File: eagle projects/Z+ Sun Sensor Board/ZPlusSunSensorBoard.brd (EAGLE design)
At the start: 78 x 78 mm, 54 parts, among them J1 Power In, J2 Power Out, U1 TSV991AILT, U2 ADS7841E_2K5, U4 LM20BIM7X_NOPB, U5 TSV991AILT, U8 TSV991AILT

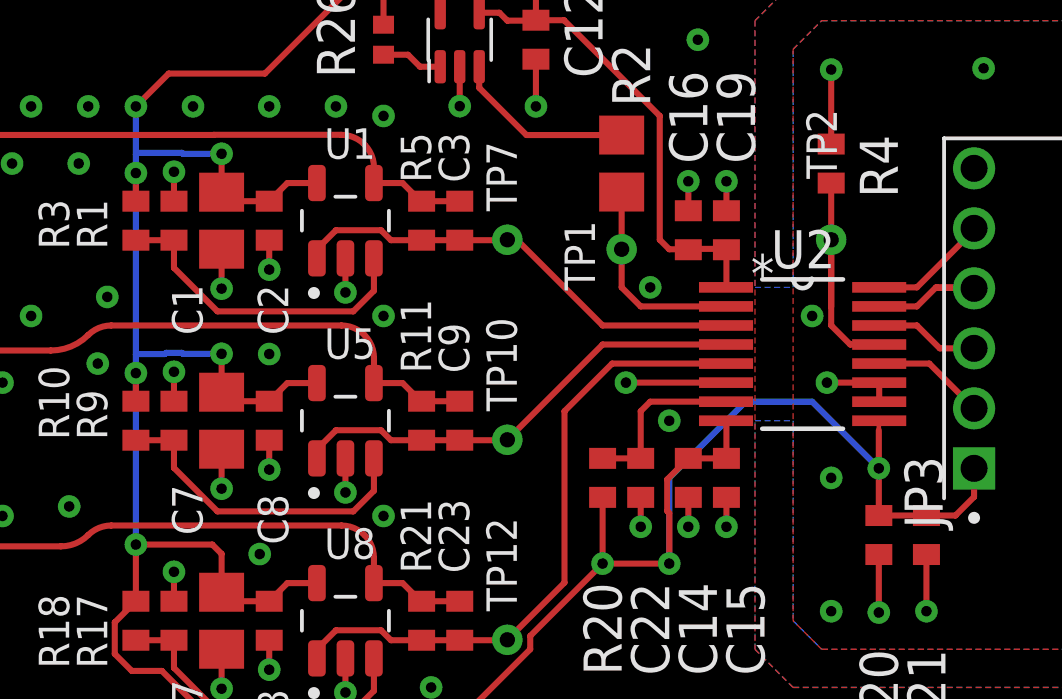
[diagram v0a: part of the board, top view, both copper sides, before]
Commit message: Cleaned up errors in Z+ and Z- boards
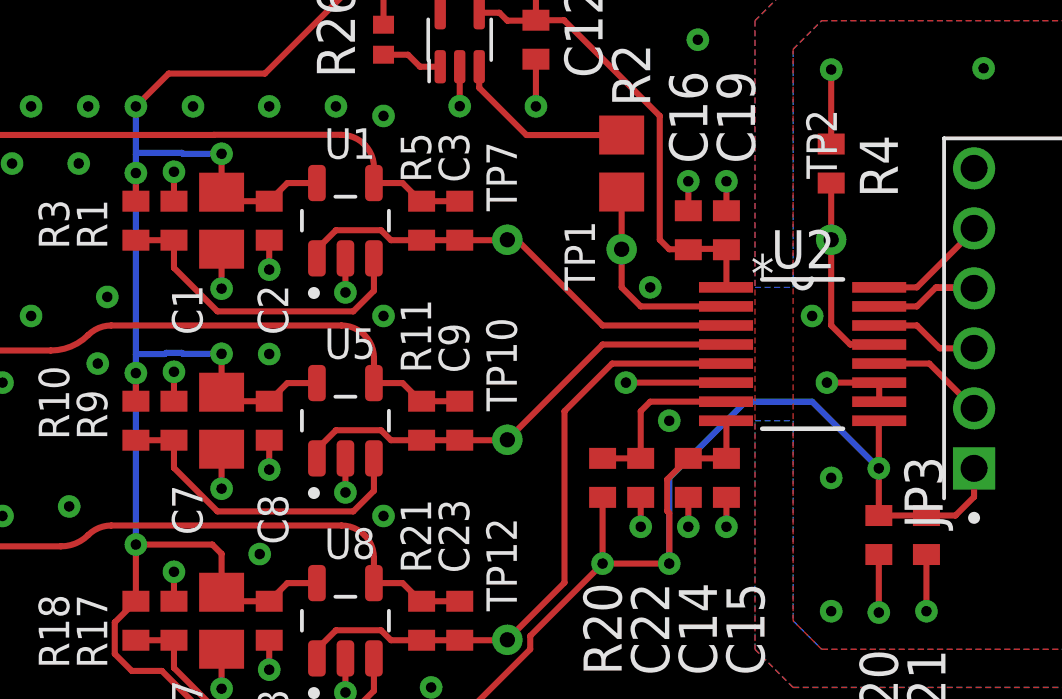
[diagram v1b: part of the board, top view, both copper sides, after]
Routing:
- net N$2: track 8.87 -> 6.61 mm

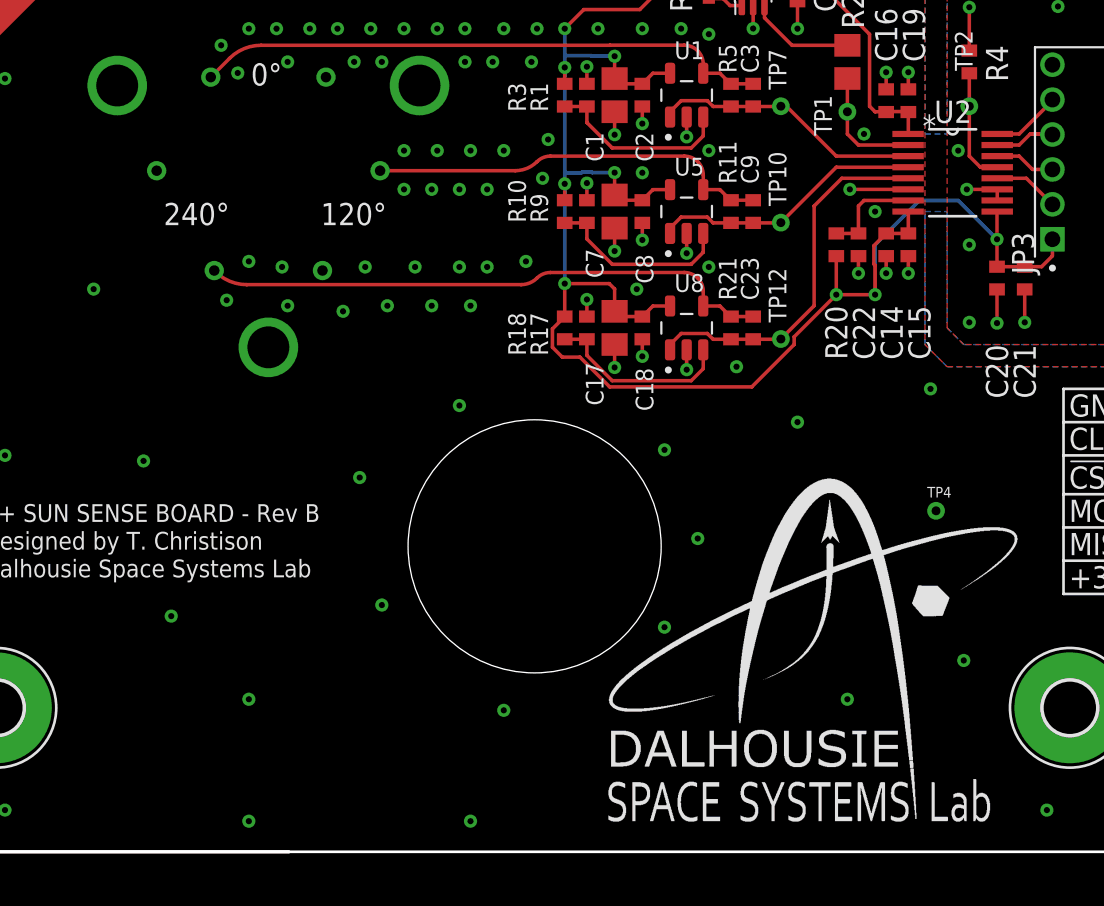
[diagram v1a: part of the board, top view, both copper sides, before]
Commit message: Air wires and wire stubs fixed on all boards
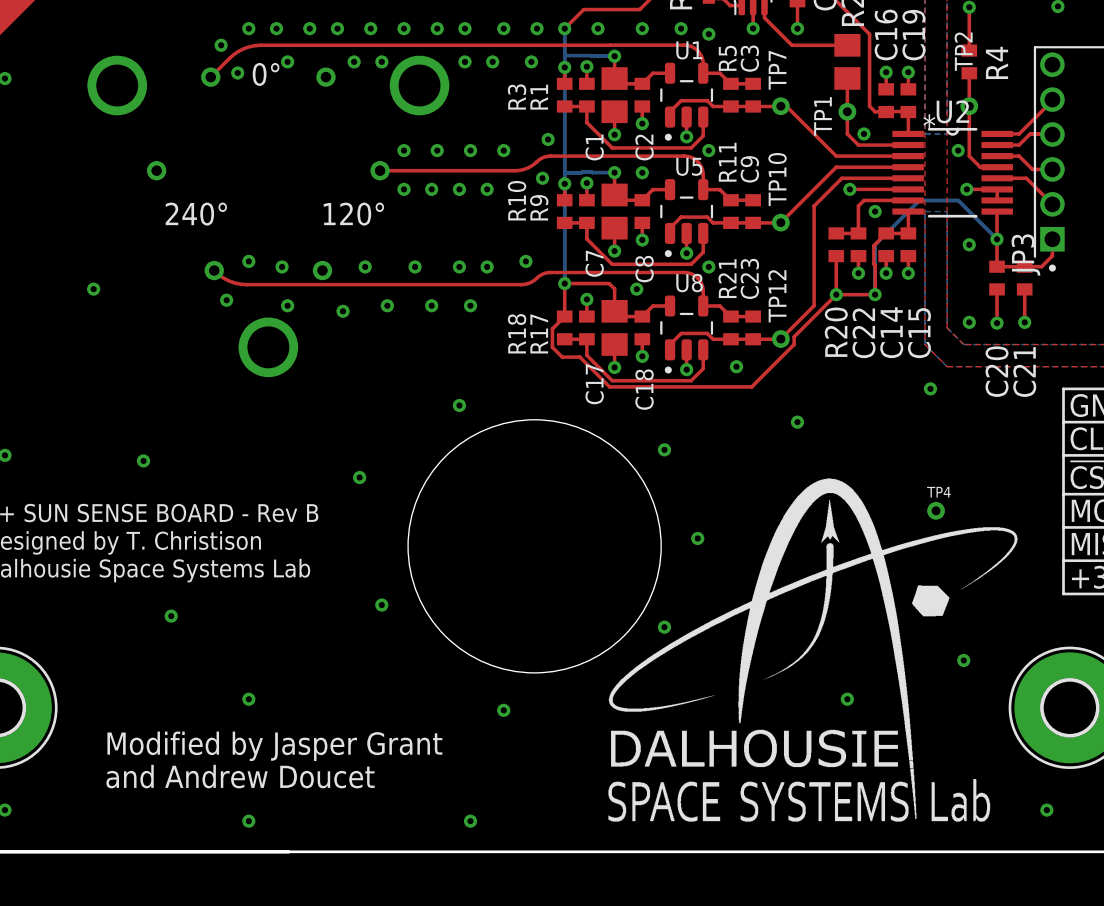
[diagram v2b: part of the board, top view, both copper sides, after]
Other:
- board text added: "Modified by Jasper Grant and Andrew Doucet"
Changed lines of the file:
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@@
 <wire x1="81.28" y1="21.2725" x2="75.8825" y2="21.2725" width="0.1524" layer="21"/>
 <wire x1="79.375" y1="33.02" x2="79.375" y2="37.465" width="0.1524" layer="21"/>
+<text x="20.955" y="10.16" size="1.27" layer="25">Modified by Jasper Grant
+and Andrew Doucet</text>
 </plain>
 <attributes>
@@
 <contactref element="C21" pad="1"/>
 <contactref element="C20" pad="1"/>
-<wire x1="72.0852" y1="43.18" x2="72.0852" y2="43.1673" width="0.2032" layer="1"/>
 <contactref element="U2" pad="1"/>
 <contactref element="C19" pad="1"/>
@@
 <signal name="N$8">
 <contactref element="R1" pad="2"/>
-<wire x1="48.5775" y1="49.1975" x2="48.88" y2="49.1975" width="0.2032" layer="1"/>
 <wire x1="47.3075" y1="49.1975" x2="48.5775" y2="49.1975" width="0.2032" layer="1"/>
-<wire x1="48.5775" y1="49.1975" x2="48.5775" y2="48.27533125" width="0.2032" layer="1"/>
 <contactref element="U1" pad="3"/>
 <wire x1="50.02813125" y1="46.8247" x2="54.55436875" y2="46.8247" width="0.2032" layer="1"/>
@@
 <wire x1="55.2425" y1="47.51283125" x2="55.2425" y2="48.5925" width="0.2032" layer="1"/>
 <contactref element="R3" pad="1"/>
+<wire x1="48.5775" y1="49.1975" x2="48.5775" y2="48.27533125" width="0.2032" layer="1"/>
 </signal>
 <signal name="+3V6">
@@
 </drawing>
 <compatibility>
+<note version="6.3" minversion="6.2.2" severity="warning">
+Since Version 6.2.2 text objects can contain more than one line,
+which will not be processed correctly with this version.
+</note>
 <note version="8.2" severity="warning">
 Since Version 8.2, EAGLE supports online libraries. The ids

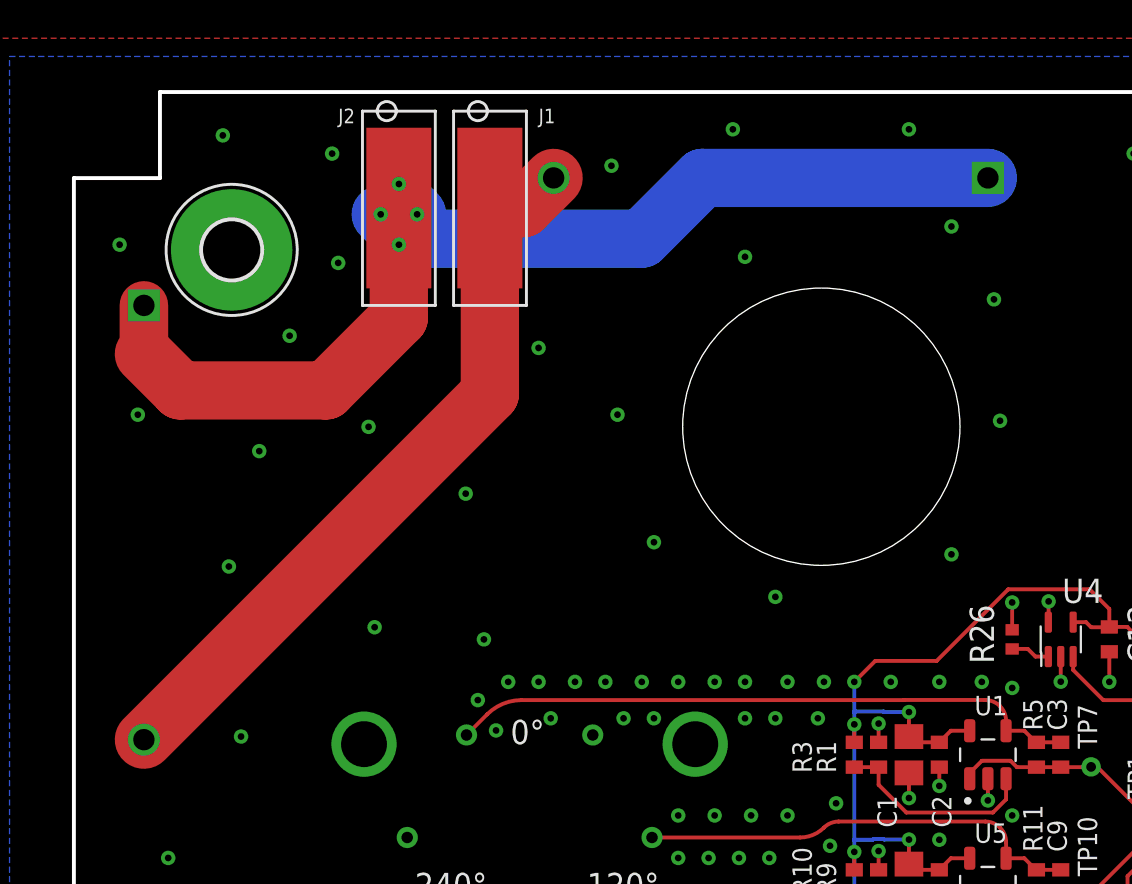
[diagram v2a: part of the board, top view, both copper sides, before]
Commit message: Added Luc's recommended new power connectors
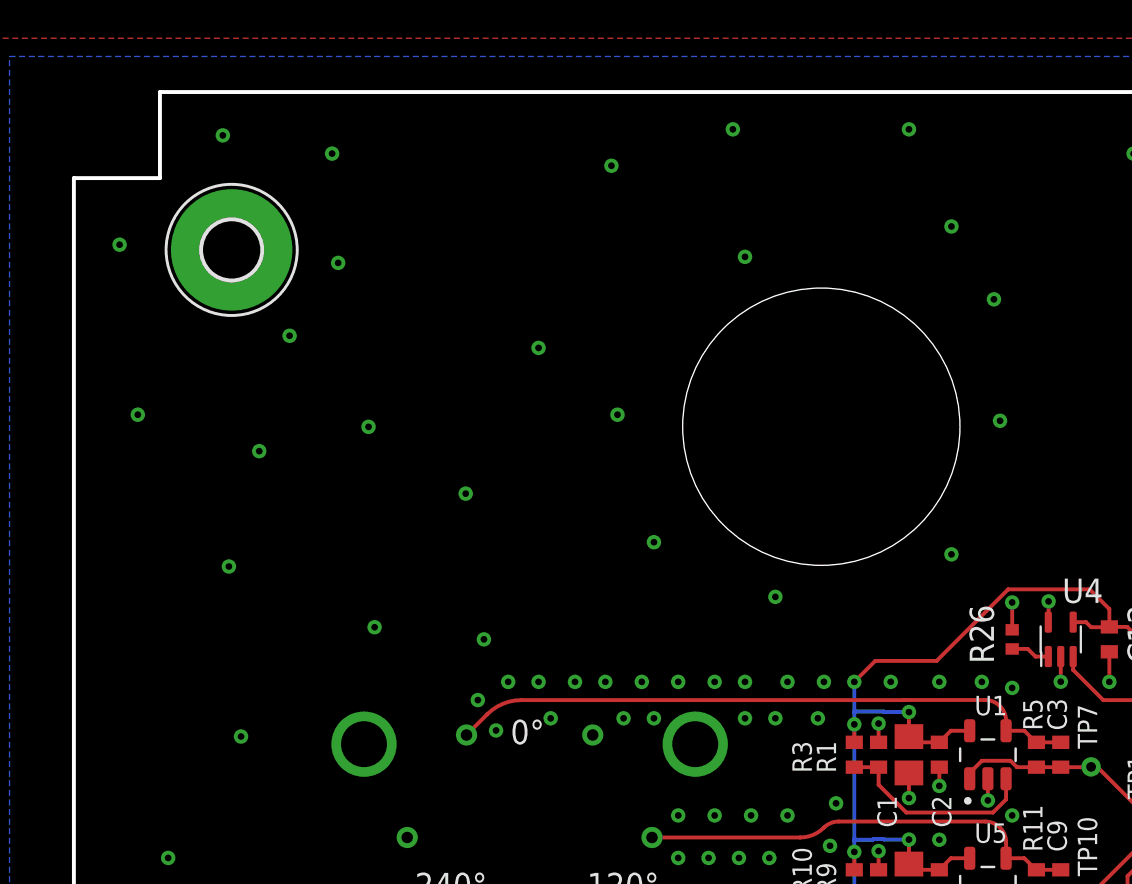
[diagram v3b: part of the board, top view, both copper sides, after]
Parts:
- removed J1: Power In, PDUv1:2038638103
- removed J2: Power Out, PDUv1:2038638103
- removed R6, R7: RS02B2R000FE70, Heating Element:ROX02B_VIS
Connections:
- removed net N$5: J1.P$1, R6.2, R7.2
- removed net N$6: J2.P$1, R6.1, R7.1
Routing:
- net N$6: track 61.1 -> 0.00 mm, vias 4 -> 0
- net N$5: track 39.3 -> 0.00 mm
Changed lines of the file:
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@@
 <element name="U$3" library="my_library" library_urn="urn:adsk.eagle:library:22876504" package="PHOTODIODE_SILK" package3d_urn="urn:adsk.eagle:package:29580099/1" value="" x="30.48" y="62.865" smashed="yes" rot="MR180"/>
 <element name="U$4" library="my_library" library_urn="urn:adsk.eagle:library:22876504" package="PHOTODIODE_SILK" package3d_urn="urn:adsk.eagle:package:29580099/1" value="" x="45.4025" y="36.5125" smashed="yes" rot="MR300"/>
-<element name="R6" library="Heating Element" library_urn="urn:adsk.eagle:library:29300905" package="ROX02B_VIS" package3d_urn="urn:adsk.eagle:package:29301001/2" value="RS02B2R000FE70" x="54.2925" y="80.01" smashed="yes" rot="MR0">
-<attribute name="BUILT_BY" value="EMA_UL_Team" x="54.2925" y="80.01" size="1.778" layer="28" rot="MR0" display="off"/>
-<attribute name="MANUFACTURER_PART_NUMBER" value="RS02B2R000FE70" x="54.2925" y="80.01" size="1.778" layer="28" rot="MR0" display="off"/>
-<attribute name="NAME" x="48.1203" y="79.375" size="1.27" layer="26" ratio="6" rot="SMR0"/>
-<attribute name="SOURCELIBRARY" value="Vishay_2014-12-31" x="54.2925" y="80.01" size="1.778" layer="28" rot="MR0" display="off"/>
-<attribute name="VENDOR" value="Vishay" x="54.2925" y="80.01" size="1.778" layer="28" rot="MR0" display="off"/>
-</element>
-<element name="R7" library="Heating Element" library_urn="urn:adsk.eagle:library:29300905" package="ROX02B_VIS" package3d_urn="urn:adsk.eagle:package:29301001/2" value="RS02B2R000FE70" x="10.16" y="73.3425" smashed="yes" rot="MR270">
-<attribute name="BUILT_BY" value="EMA_UL_Team" x="10.16" y="73.3425" size="1.778" layer="28" rot="MR270" display="off"/>
-<attribute name="MANUFACTURER_PART_NUMBER" value="RS02B2R000FE70" x="10.16" y="73.3425" size="1.778" layer="28" rot="MR270" display="off"/>
-<attribute name="NAME" x="10.79499375" y="65.2653" size="1.27" layer="26" ratio="6" rot="SMR270"/>
-<attribute name="SOURCELIBRARY" value="Vishay_2014-12-31" x="10.16" y="73.3425" size="1.778" layer="28" rot="MR270" display="off"/>
-<attribute name="VENDOR" value="Vishay" x="10.16" y="73.3425" size="1.778" layer="28" rot="MR270" display="off"/>
-</element>
-<element name="J1" library="PDUv1" library_urn="urn:adsk.eagle:library:29653418" package="2038638103" package3d_urn="urn:adsk.eagle:package:30104253/5" value="Power In" x="26.3525" y="82.2325" smashed="yes" rot="R270">
-<attribute name="NAME" x="30.7975" y="82.8675" size="0.762" layer="25"/>
-<attribute name="VALUE" x="26.67" y="72.39" size="0.762" layer="27"/>
-</element>
-<element name="J2" library="PDUv1" library_urn="urn:adsk.eagle:library:29653418" package="2038638103" package3d_urn="urn:adsk.eagle:package:30104253/5" value="Power Out" x="21.59" y="82.2325" smashed="yes" rot="R270">
-<attribute name="NAME" x="20.32" y="82.8675" size="0.762" layer="25"/>
-<attribute name="VALUE" x="20.6375" y="72.39" size="0.762" layer="27"/>
-</element>
 <element name="JP3" library="830-10-006-20-005000" package="830-10-006-20-005000" value="830-10-006-20-005000" x="75.2475" y="41.5925" smashed="yes" rot="R90">
 <attribute name="AVAILABILITY" value="In Stock" x="75.2475" y="41.5925" size="1.778" layer="27" rot="R90" display="off"/>
@@
 <wire x1="48.5775" y1="35.8625" x2="48.5775" y2="34.94033125" width="0.2032" layer="1"/>
 </signal>
-<signal name="N$5">
-<contactref element="R6" pad="2"/>
-<contactref element="R7" pad="2"/>
-<contactref element="J1" pad="P$1"/>
-<wire x1="31.5849" y1="80.01" x2="30.0074" y2="78.4325" width="3.048" layer="1"/>
-<wire x1="30.0074" y1="78.4325" x2="28.2525" y2="78.4325" width="3.048" layer="1"/>
-<wire x1="28.2525" y1="78.4325" x2="28.2525" y2="68.7274" width="3.048" layer="1"/>
-<wire x1="28.2525" y1="68.7274" x2="10.16" y2="50.6349" width="3.048" layer="1"/>
-</signal>
-<signal name="N$6">
-<contactref element="R6" pad="1"/>
-<contactref element="R7" pad="1"/>
-<via x="23.495" y="79.6925" extent="1-16" drill="0.35"/>
-<via x="24.4475" y="78.105" extent="1-16" drill="0.35"/>
-<via x="23.495" y="76.5175" extent="1-16" drill="0.35"/>
-<via x="22.5425" y="78.105" extent="1-16" drill="0.35"/>
-<wire x1="39.37" y1="80.01" x2="36.195" y2="76.835" width="3.048" layer="16"/>
-<wire x1="36.195" y1="76.835" x2="25.0825" y2="76.835" width="3.048" layer="16"/>
-<wire x1="25.0825" y1="76.835" x2="23.1775" y2="78.74" width="3.048" layer="16"/>
-<wire x1="54.2925" y1="80.01" x2="39.37" y2="80.01" width="3.048" layer="16"/>
-<wire x1="22.5425" y1="78.105" x2="23.495" y2="77.1525" width="3.048" layer="16"/>
-<wire x1="23.495" y1="77.1525" x2="23.495" y2="76.5175" width="3.048" layer="16"/>
-<wire x1="23.495" y1="79.6925" x2="23.495" y2="79.0575" width="3.048" layer="16"/>
-<wire x1="23.495" y1="79.0575" x2="24.4475" y2="78.105" width="3.048" layer="16"/>
-<contactref element="J2" pad="P$1"/>
-<wire x1="23.49" y1="72.7025" x2="19.685" y2="68.8975" width="3.048" layer="1"/>
-<wire x1="23.49" y1="72.7025" x2="23.49" y2="78.4325" width="3.048" layer="1"/>
-<wire x1="12.065" y1="68.8975" x2="10.16" y2="70.8025" width="3.048" layer="1"/>
-<wire x1="19.685" y1="68.8975" x2="12.065" y2="68.8975" width="3.048" layer="1"/>
-<wire x1="10.16" y1="70.8025" x2="10.16" y2="73.3425" width="2.54" layer="1"/>
-<wire x1="23.49" y1="78.4325" x2="23.1775" y2="78.74" width="0" layer="19" extent="1-16"/>
-<wire x1="22.5425" y1="78.105" x2="23.1775" y2="78.74" width="0" layer="19" extent="16-16"/>
-<wire x1="23.495" y1="79.6925" x2="23.1775" y2="78.74" width="0" layer="19" extent="16-16"/>
-</signal>
 <signal name="N$94">
